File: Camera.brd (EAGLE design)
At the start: 30 x 60 mm, 53 parts, among them SW1 THAU13-AB-R, SW2 THAU13-AB-R, SW3 TVAF06-A020B-R, SW4 TVAF06-A020B-R, U1 I-02247_NJM2845, U2 DRIVER-LV8548MC-AH(SOIC10), U3 OPA340N, U4 NJM11100, U5 NJM11100

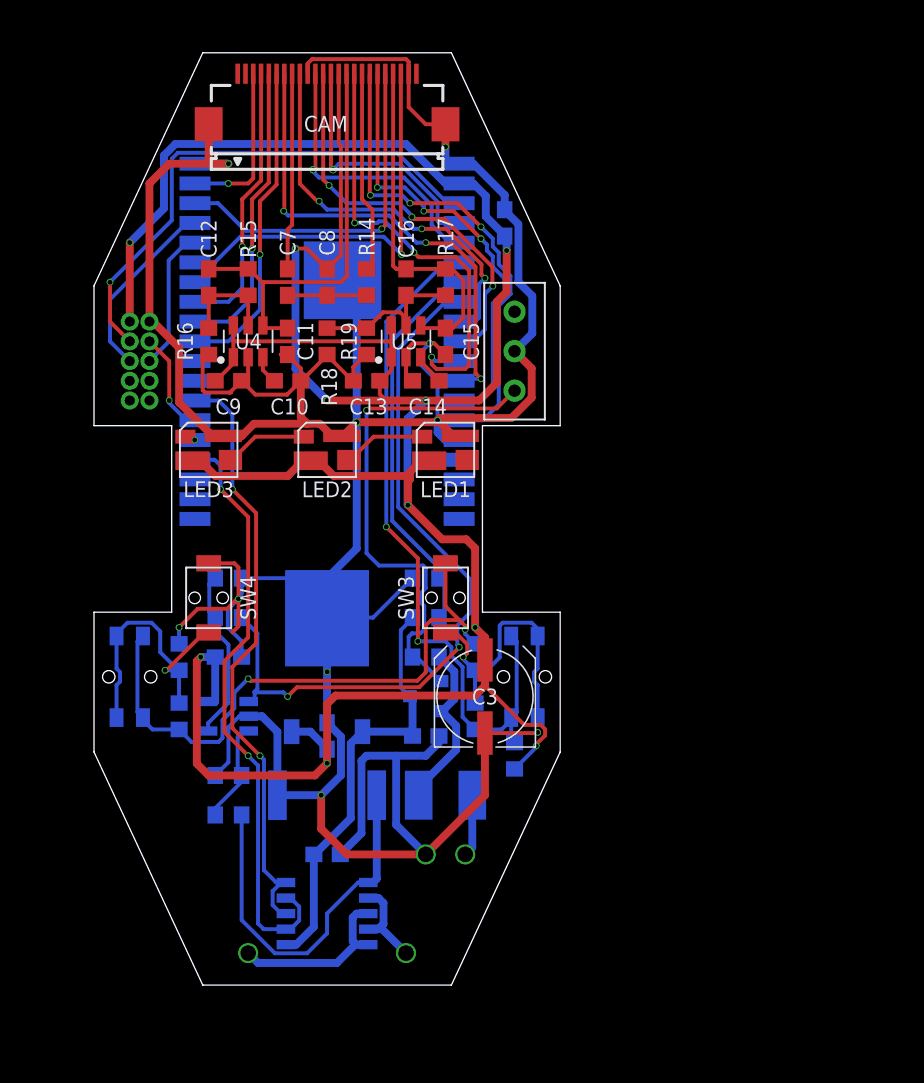
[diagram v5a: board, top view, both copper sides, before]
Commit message: Add GND plane
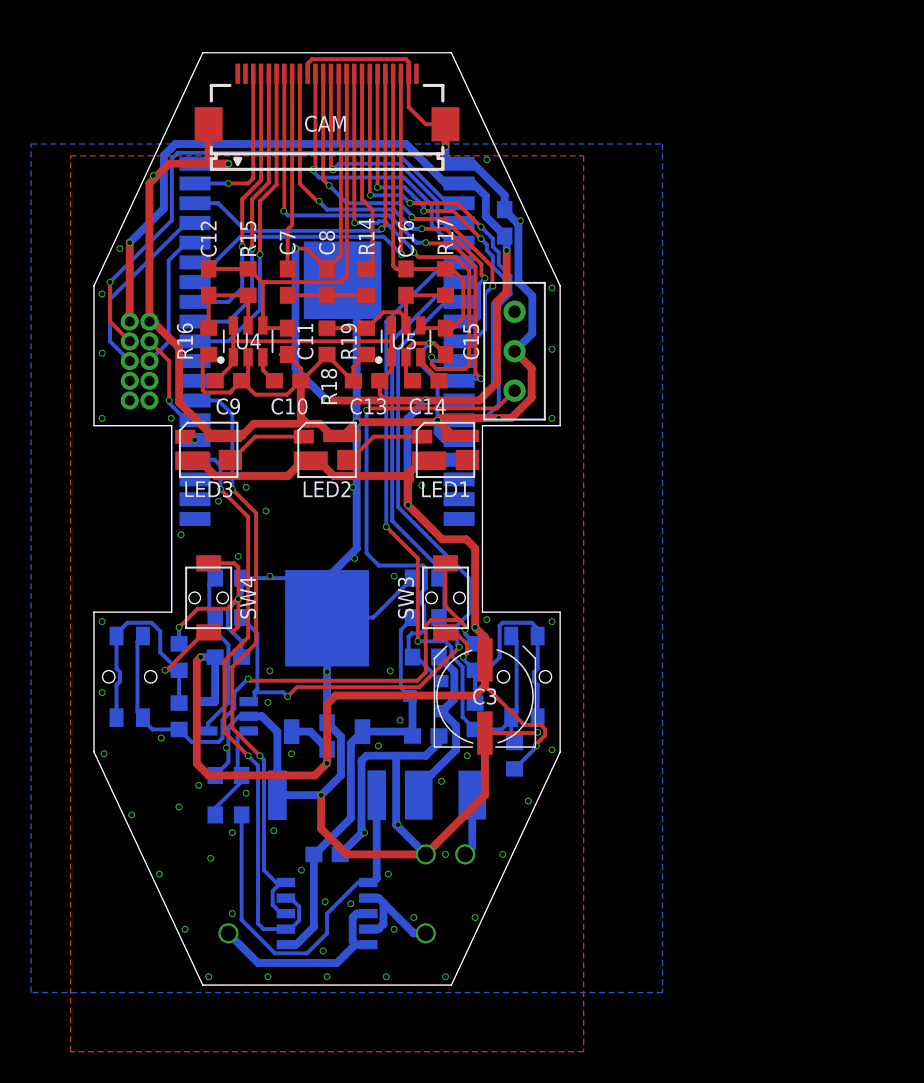
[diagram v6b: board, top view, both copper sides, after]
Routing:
- net M1: track 11.4 -> 13.2 mm
- net M2: track 5.93 -> 7.11 mm
- net GND: vias 11 -> 77
- added copper zone on layer 1, net GND
- added copper zone on layer 16, net GND
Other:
- board text added: "2022 WASA Rocket"
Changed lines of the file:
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@@
 <layer number="14" name="Route14" color="22" fill="1" visible="no" active="no"/>
 <layer number="15" name="Route15" color="23" fill="1" visible="no" active="no"/>
-<layer number="16" name="Bottom" color="1" fill="1" visible="no" active="yes"/>
+<layer number="16" name="Bottom" color="1" fill="1" visible="yes" active="yes"/>
 <layer number="17" name="Pads" color="2" fill="1" visible="yes" active="yes"/>
 <layer number="18" name="Vias" color="2" fill="1" visible="yes" active="yes"/>
@@
 <layer number="20" name="Dimension" color="24" fill="1" visible="yes" active="yes"/>
 <layer number="21" name="tPlace" color="7" fill="1" visible="yes" active="yes"/>
-<layer number="22" name="bPlace" color="7" fill="1" visible="no" active="yes"/>
+<layer number="22" name="bPlace" color="7" fill="1" visible="yes" active="yes"/>
 <layer number="23" name="tOrigins" color="15" fill="1" visible="yes" active="yes"/>
-<layer number="24" name="bOrigins" color="15" fill="1" visible="no" active="yes"/>
+<layer number="24" name="bOrigins" color="15" fill="1" visible="yes" active="yes"/>
 <layer number="25" name="tNames" color="7" fill="1" visible="yes" active="yes"/>
-<layer number="26" name="bNames" color="7" fill="1" visible="no" active="yes"/>
+<layer number="26" name="bNames" color="7" fill="1" visible="yes" active="yes"/>
 <layer number="27" name="tValues" color="7" fill="1" visible="no" active="yes"/>
 <layer number="28" name="bValues" color="7" fill="1" visible="no" active="yes"/>
-<layer number="29" name="tStop" color="7" fill="3" visible="no" active="yes"/>
+<layer number="29" name="tStop" color="7" fill="3" visible="yes" active="yes"/>
 <layer number="30" name="bStop" color="7" fill="6" visible="no" active="yes"/>
 <layer number="31" name="tCream" color="7" fill="4" visible="no" active="yes"/>
@@
 <layer number="38" name="bTest" color="7" fill="1" visible="no" active="yes"/>
 <layer number="39" name="tKeepout" color="4" fill="11" visible="yes" active="yes"/>
-<layer number="40" name="bKeepout" color="1" fill="11" visible="no" active="yes"/>
+<layer number="40" name="bKeepout" color="1" fill="11" visible="yes" active="yes"/>
 <layer number="41" name="tRestrict" color="4" fill="10" visible="yes" active="yes"/>
-<layer number="42" name="bRestrict" color="1" fill="10" visible="no" active="yes"/>
+<layer number="42" name="bRestrict" color="1" fill="10" visible="yes" active="yes"/>
 <layer number="43" name="vRestrict" color="2" fill="10" visible="no" active="yes"/>
 <layer number="44" name="Drills" color="7" fill="1" visible="no" active="yes"/>
@@
 <layer number="50" name="dxf" color="7" fill="1" visible="no" active="no"/>
 <layer number="51" name="tDocu" color="7" fill="1" visible="yes" active="yes"/>
-<layer number="52" name="bDocu" color="7" fill="1" visible="no" active="yes"/>
+<layer number="52" name="bDocu" color="7" fill="1" visible="yes" active="yes"/>
 <layer number="53" name="tGND_GNDA" color="7" fill="1" visible="no" active="no"/>
 <layer number="54" name="bGND_GNDA" color="7" fill="1" visible="no" active="no"/>
@@
 <wire x1="6" y1="-27" x2="-6" y2="-27" width="0.127" layer="51"/>
 <wire x1="-6" y1="-27" x2="-6" y2="-3" width="0.127" layer="51"/>
+<text x="0" y="-28.321" size="1.27" layer="29" font="vector" ratio="10" align="center">2022 WASA Rocket</text>
 </plain>
 <attributes>
@@
 <wire x1="7.112" y1="8.846425" x2="7.112" y2="6.35" width="0.254" layer="16"/>
 <wire x1="5.969" y1="10.668" x2="5.969" y2="9.989425" width="0.254" layer="16"/>
-<wire x1="0" y1="14.36" x2="0" y2="14.39" width="0" layer="19" extent="1-16"/>
+<polygon width="0" layer="16">
+<vertex x="21.59" y="24.13"/>
+<vertex x="21.59" y="24.13"/>
+<vertex x="21.59" y="-30.48"/>
+<vertex x="-19.05" y="-30.48"/>
+<vertex x="-19.05" y="24.13"/>
+</polygon>
+<polygon width="0" layer="1">
+<vertex x="16.51" y="23.368"/>
+<vertex x="16.51" y="-34.29"/>
+<vertex x="-16.51" y="-34.29"/>
+<vertex x="-16.51" y="23.368"/>
+</polygon>
+<via x="11.049" y="6.477" extent="1-16" drill="0.3"/>
+<via x="14.478" y="6.477" extent="1-16" drill="0.3"/>
+<via x="14.478" y="10.922" extent="1-16" drill="0.3"/>
+<via x="14.478" y="14.859" extent="1-16" drill="0.3"/>
+<via x="12.446" y="19.177" extent="1-16" drill="0.3"/>
+<via x="10.287" y="23.114" extent="1-16" drill="0.3"/>
+<via x="-11.176" y="22.098" extent="1-16" drill="0.3"/>
+<via x="-13.335" y="17.399" extent="1-16" drill="0.3"/>
+<via x="-14.478" y="14.478" extent="1-16" drill="0.3"/>
+<via x="-14.478" y="10.668" extent="1-16" drill="0.3"/>
+<via x="-14.478" y="6.477" extent="1-16" drill="0.3"/>
+<via x="-10.033" y="6.477" extent="1-16" drill="0.3"/>
+<via x="6.096" y="2.159" extent="1-16" drill="0.3"/>
+<via x="1.651" y="2.032" extent="1-16" drill="0.3"/>
+<via x="-5.207" y="2.032" extent="1-16" drill="0.3"/>
+<via x="-3.937" y="0.508" extent="1-16" drill="0.3"/>
+<via x="-6.985" y="1.143" extent="1-16" drill="0.3"/>
+<via x="-9.398" y="-1.016" extent="1-16" drill="0.3"/>
+<via x="-5.715" y="-2.413" extent="1-16" drill="0.3"/>
+<via x="-3.683" y="-3.683" extent="1-16" drill="0.3"/>
+<via x="1.778" y="-2.54" extent="1-16" drill="0.3"/>
+<via x="-3.683" y="-9.779" extent="1-16" drill="0.3"/>
+<via x="4.064" y="-9.779" extent="1-16" drill="0.3"/>
+<via x="4.318" y="-3.683" extent="1-16" drill="0.3"/>
+<via x="10.287" y="-6.477" extent="1-16" drill="0.3"/>
+<via x="14.478" y="-6.604" extent="1-16" drill="0.3"/>
+<via x="14.478" y="-14.859" extent="1-16" drill="0.3"/>
+<via x="12.954" y="-18.161" extent="1-16" drill="0.3"/>
+<via x="9.017" y="-15.24" extent="1-16" drill="0.3"/>
+<via x="7.366" y="-16.891" extent="1-16" drill="0.3"/>
+<via x="3.302" y="-14.605" extent="1-16" drill="0.3"/>
+<via x="4.699" y="-12.954" extent="1-16" drill="0.3"/>
+<via x="-3.81" y="-11.811" extent="1-16" drill="0.3"/>
+<via x="-2.286" y="-15.113" extent="1-16" drill="0.3"/>
+<via x="-6.477" y="-14.732" extent="1-16" drill="0.3"/>
+<via x="-10.668" y="-14.097" extent="1-16" drill="0.3"/>
+<via x="-14.478" y="-6.604" extent="1-16" drill="0.3"/>
+<via x="-14.478" y="-11.176" extent="1-16" drill="0.3"/>
+<via x="-14.351" y="-15.113" extent="1-16" drill="0.3"/>
+<via x="-12.573" y="-19.05" extent="1-16" drill="0.3"/>
+<via x="-9.525" y="-18.542" extent="1-16" drill="0.3"/>
+<via x="-8.255" y="-17.145" extent="1-16" drill="0.3"/>
+<via x="-5.207" y="-17.653" extent="1-16" drill="0.3"/>
+<via x="-3.429" y="-20.066" extent="1-16" drill="0.3"/>
+<via x="4.572" y="-19.685" extent="1-16" drill="0.3"/>
+<via x="2.413" y="-20.193" extent="1-16" drill="0.3"/>
+<via x="7.62" y="-21.59" extent="1-16" drill="0.3"/>
+<via x="11.303" y="-21.59" extent="1-16" drill="0.3"/>
+<via x="9.525" y="-25.654" extent="1-16" drill="0.3"/>
+<via x="3.937" y="-22.86" extent="1-16" drill="0.3"/>
+<via x="5.588" y="-25.654" extent="1-16" drill="0.3"/>
+<via x="1.524" y="-24.765" extent="1-16" drill="0.3"/>
+<via x="-0.127" y="-24.638" extent="1-16" drill="0.3"/>
+<via x="-1.651" y="-22.606" extent="1-16" drill="0.3"/>
+<via x="4.318" y="-26.416" extent="1-16" drill="0.3"/>
+<via x="7.62" y="-29.464" extent="1-16" drill="0.3"/>
+<via x="3.81" y="-29.464" extent="1-16" drill="0.3"/>
+<via x="-0.254" y="-27.813" extent="1-16" drill="0.3"/>
+<via x="0" y="-29.464" extent="1-16" drill="0.3"/>
+<via x="-3.81" y="-29.464" extent="1-16" drill="0.3"/>
+<via x="-7.62" y="-29.464" extent="1-16" drill="0.3"/>
+<via x="-9.144" y="-26.416" extent="1-16" drill="0.3"/>
+<via x="-6.096" y="-25.4" extent="1-16" drill="0.3"/>
+<via x="-7.493" y="-21.844" extent="1-16" drill="0.3"/>
+<via x="-10.795" y="-22.86" extent="1-16" drill="0.3"/>
+<via x="-6.096" y="-20.193" extent="1-16" drill="0.3"/>
 </signal>
 <signal name="VDD">
@@
 <contactref element="U2" pad="10"/>
 <contactref element="U2" pad="8"/>
-<via x="-5.08" y="-27.94" extent="1-16" drill="1" diameter="1.3" alwaysstop="yes"/>
+<via x="-6.35" y="-26.67" extent="1-16" drill="1" diameter="1.3" alwaysstop="yes"/>
 <wire x1="2.65" y1="-25.4" x2="1.905" y2="-25.4" width="0.508" layer="16"/>
 <wire x1="1.905" y1="-25.4" x2="1.651" y2="-25.654" width="0.508" layer="16"/>
@@
 <wire x1="1.651" y1="-27.178" x2="1.873" y2="-27.4" width="0.508" layer="16"/>
 <wire x1="1.873" y1="-27.4" x2="1.81" y2="-27.4" width="0.508" layer="16"/>
-<wire x1="-4.445" y1="-28.575" x2="-5.08" y2="-27.94" width="0.508" layer="16"/>
+<wire x1="-4.445" y1="-28.575" x2="-6.35" y2="-26.67" width="0.508" layer="16"/>
 <wire x1="1.81" y1="-27.4" x2="0.635" y2="-28.575" width="0.508" layer="16"/>
 <wire x1="0.635" y1="-28.575" x2="-4.445" y2="-28.575" width="0.508" layer="16"/>
@@
 <contactref element="U2" pad="7"/>
 <contactref element="U2" pad="9"/>
-<via x="5.08" y="-27.94" extent="1-16" drill="1" diameter="1.3" alwaysstop="yes"/>
+<via x="6.35" y="-26.67" extent="1-16" drill="1" diameter="1.3" alwaysstop="yes"/>
 <wire x1="2.65" y1="-26.4" x2="3.309209375" y2="-26.4" width="0.508" layer="16"/>
-<wire x1="3.309209375" y1="-26.4" x2="3.42460625" y2="-26.284603125" width="0.508" layer="16"/>
-<wire x1="3.42460625" y1="-26.284603125" x2="3.631" y2="-26.078209375" width="0.508" layer="16"/>
+<wire x1="3.309209375" y1="-26.4" x2="3.631" y2="-26.078209375" width="0.508" layer="16"/>
 <wire x1="3.631" y1="-26.078209375" x2="3.631" y2="-24.721790625" width="0.508" layer="16"/>
 <wire x1="3.631" y1="-24.721790625" x2="3.309209375" y2="-24.4" width="0.508" layer="16"/>
 <wire x1="3.309209375" y1="-24.4" x2="2.65" y2="-24.4" width="0.508" layer="16"/>
-<wire x1="3.42460625" y1="-26.284603125" x2="3.42460625" y2="-26.28460625" width="0.508" layer="16"/>
-<wire x1="3.42460625" y1="-26.28460625" x2="5.08" y2="-27.94" width="0.508" layer="16"/>
+<wire x1="6.35" y1="-26.67" x2="5.579215625" y2="-26.67000625" width="0.508" layer="16"/>
+<wire x1="5.579215625" y1="-26.67000625" x2="3.631" y2="-24.721790625" width="0.508" layer="16"/>
 </signal>
 <signal name="MC1">
